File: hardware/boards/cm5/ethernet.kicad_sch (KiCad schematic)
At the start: 6 parts, among them J601 HR911130A, U601 TPD4E02B04DQAR, U602 TPD4E02B04DQAR

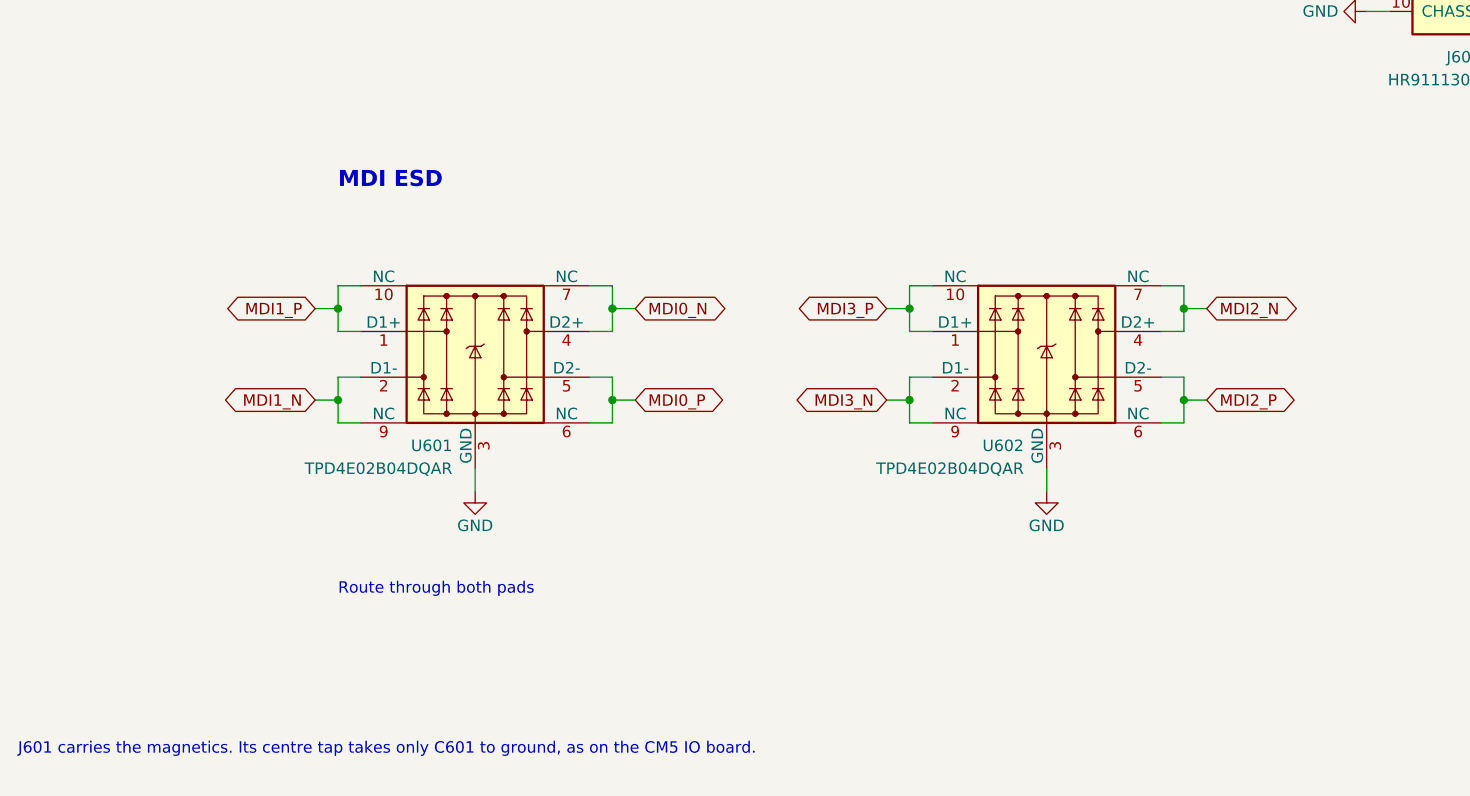
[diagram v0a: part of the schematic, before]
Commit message: feat(cm5): route the side board
Every net routed and DRC clean with schematic parity. Pairs are length matched; slow lines run as
45-degree diagonals, with In3 carrying the long cross-board runs (RPIBOOT, CM5_3V3, the PCIe
sideband, VBUS_EN) under the outer layers' high-speed walls.

The board is 102 mm deep like the main board, with five mounting holes at the corners and beside
the rear ports. The service port joins its D pins over and under the receptacle's pad row, and
U501's CC channels follow the connector's order so both CC lines run straight to R501 and R502.
The jack LED resistors sit west of the jack, R101 beside the fan header and R406 beside Q401.
The MDI pairs have no ESD array, as on the CM5 IO board. SW501's twin pin-1 pads are marked as
jumpered.
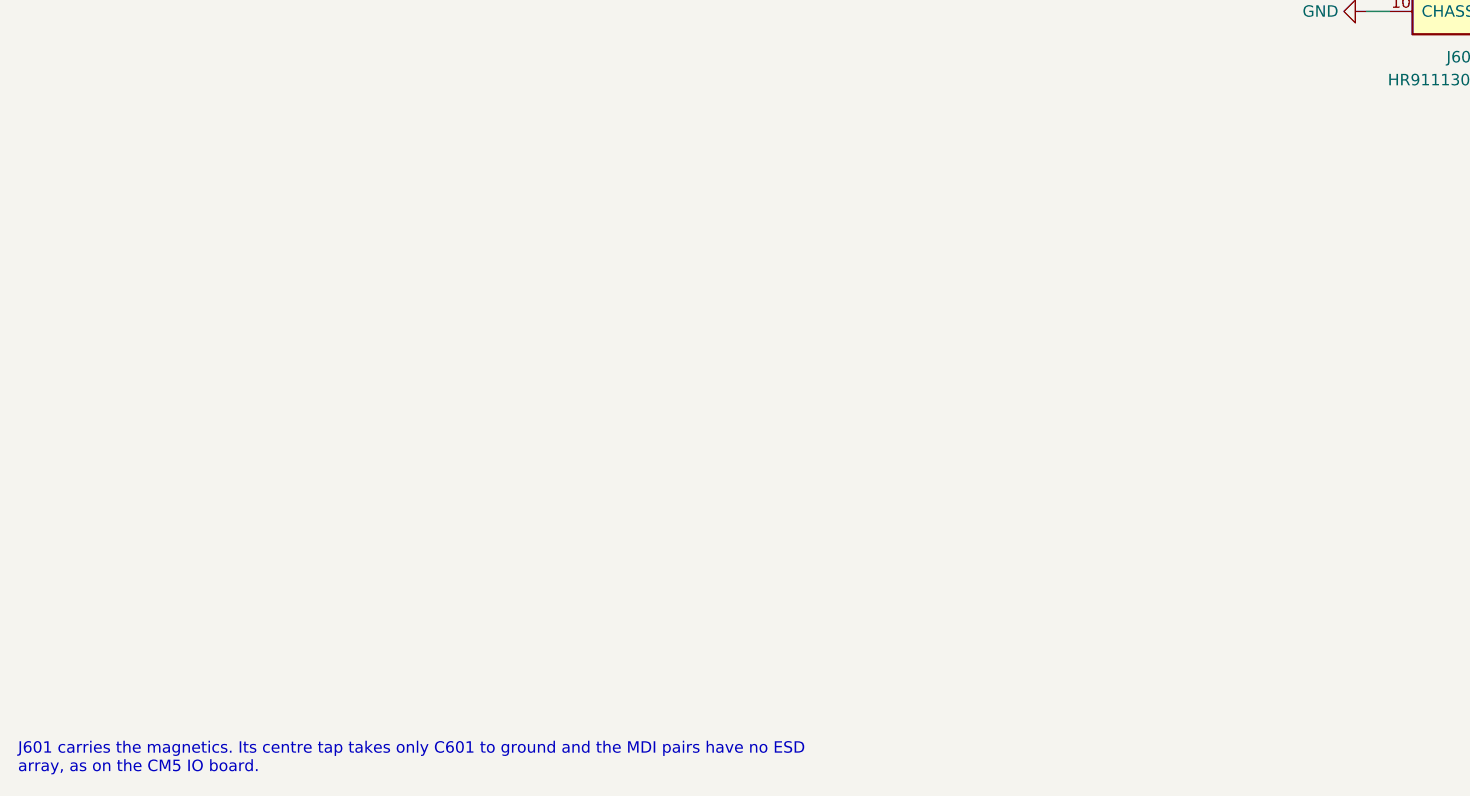
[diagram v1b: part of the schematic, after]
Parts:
- removed U601, U602: TPD4E02B04DQAR, Package_SON:USON-10_2.5x1.0mm_P0.5mm, symbol Iasis:TPD4E02B04DQA
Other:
- note added: "J601 carries the magnetics. Its centre tap takes only C601 to ground and the MDI pairs have no ESD array, as on the CM5 IO board."
- note removed: "J601 carries the magnetics. Its centre tap takes only C601 to ground, as on the CM5 IO board."
- note removed: "MDI ESD"
- note removed: "Route through both pads"
